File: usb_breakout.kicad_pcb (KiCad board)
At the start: 2 copper layers, 10.1 x 11.7 mm, 2 parts, among them X1 68710614522, X2 U-G-M5WS-W-01

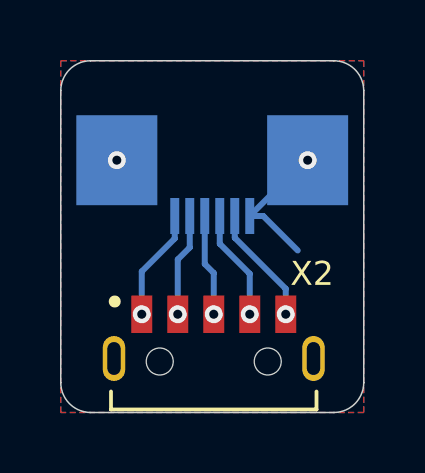
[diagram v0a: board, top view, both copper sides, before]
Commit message: usb breakout: avoid vias in pad
Signed-off-by: Marc 'risson' Schmitt <marc.schmitt@risson.space>
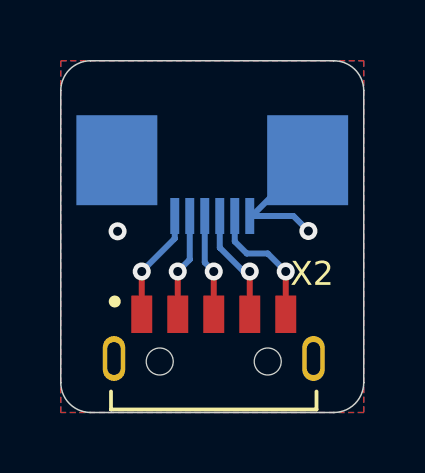
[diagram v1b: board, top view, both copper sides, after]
